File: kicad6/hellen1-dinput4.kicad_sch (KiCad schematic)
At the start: 9 parts

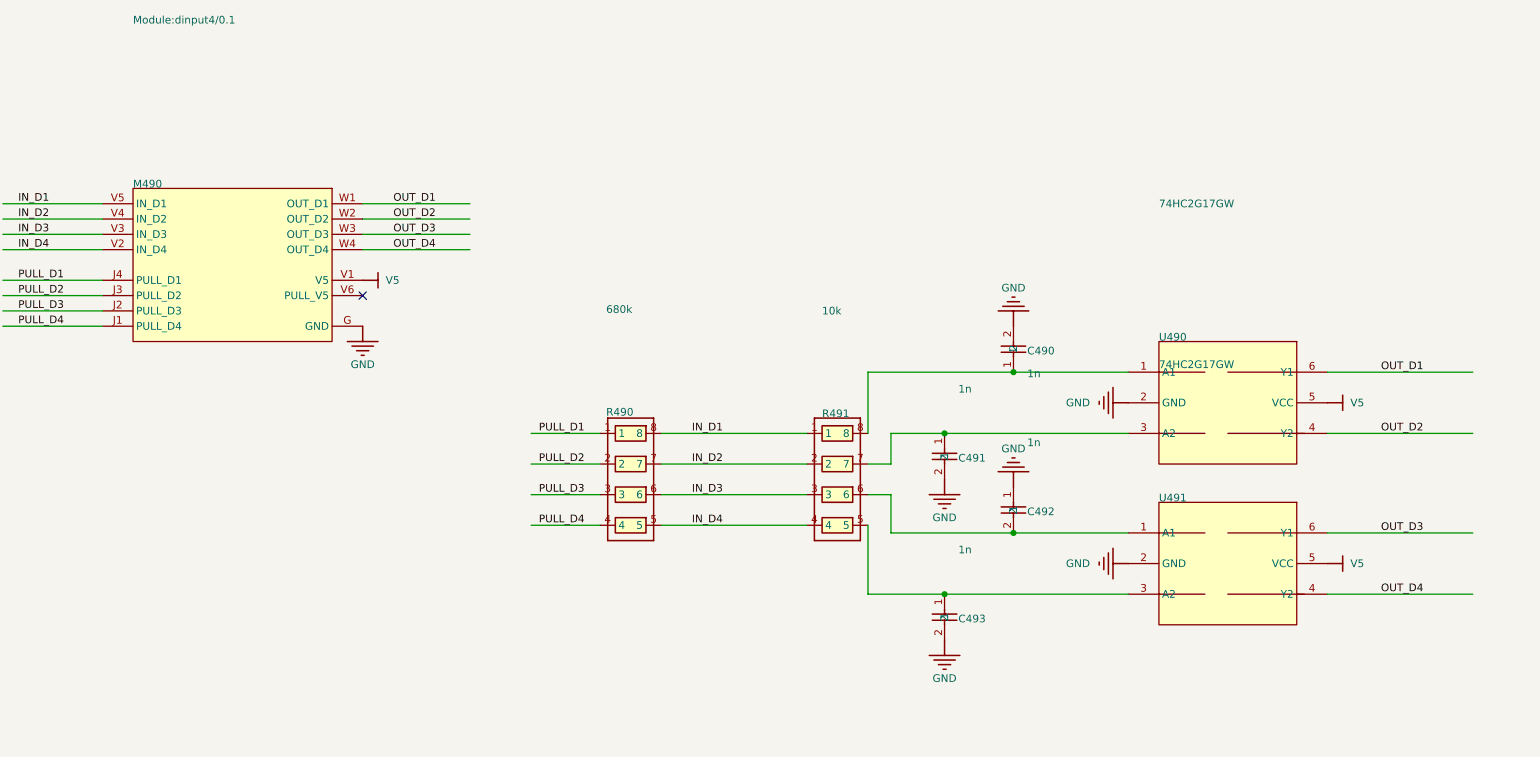
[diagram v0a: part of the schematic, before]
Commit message: move kicad src files into a separate folder
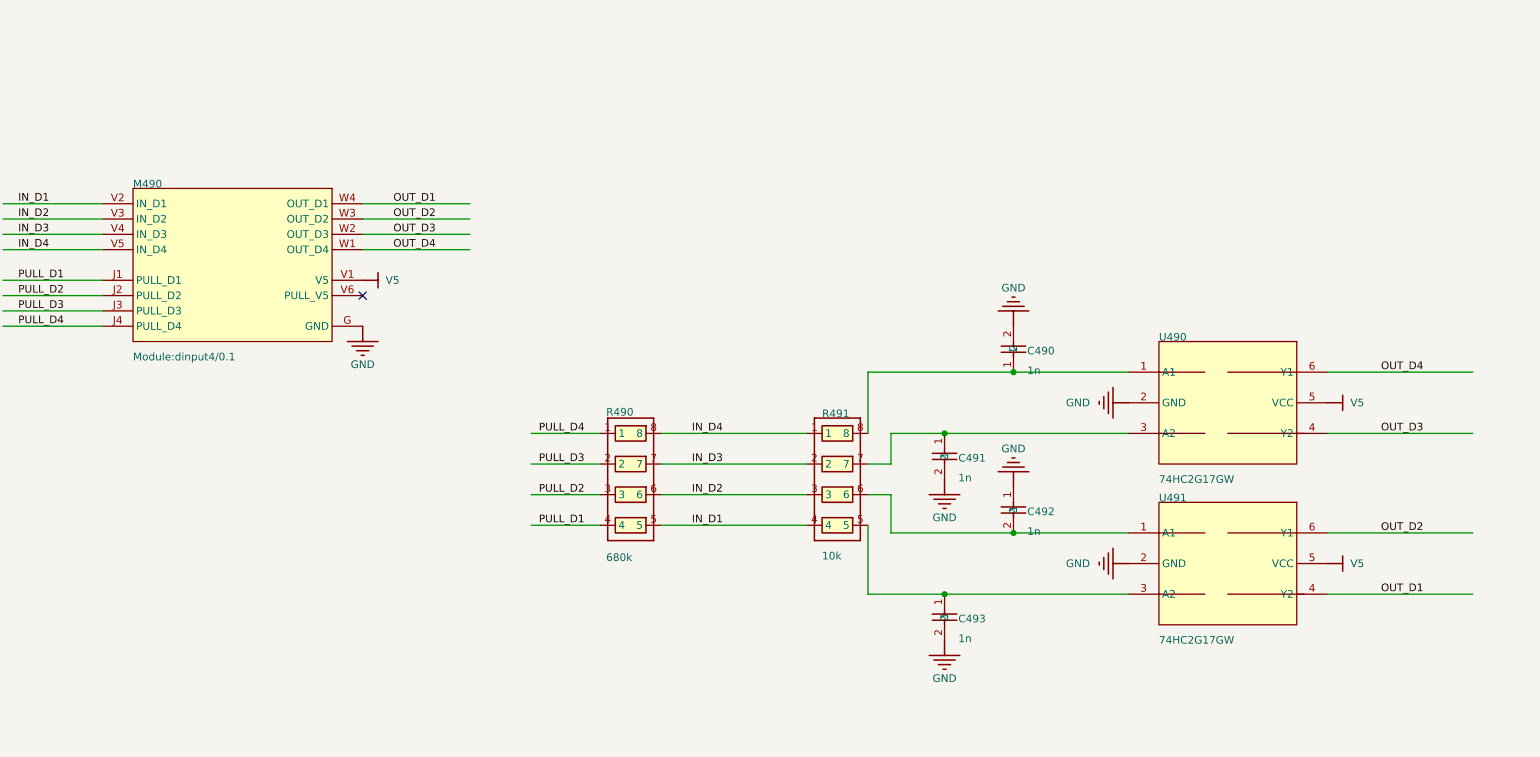
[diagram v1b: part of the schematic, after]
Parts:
- C490, C491, C492, C493: value (none) -> 1n; Comment 1n -> (none)
- M490: value (none) -> Module:dinput4/0.1; Comment Module:dinput4/0.1 -> (none)
- R490: value (none) -> 680k; Comment 680k -> (none)
- R491: value (none) -> 10k; Comment 10k -> (none)
- U490, U491: value (none) -> 74HC2G17GW; Comment 74HC2G17GW -> (none)
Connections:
- net IN_D1: now also M490.V2 (IN_D1), R490.5, R491.4; no longer M490.V5 (IN_D1), R490.8, R491.1
- net IN_D2: now also M490.V3 (IN_D2), R490.6, R491.3; no longer M490.V4 (IN_D2), R490.7, R491.2
- net IN_D3: now also M490.V4 (IN_D3), R490.7, R491.2; no longer M490.V3 (IN_D3), R490.6, R491.3
- net IN_D4: now also M490.V5 (IN_D4), R490.8, R491.1; no longer M490.V2 (IN_D4), R490.5, R491.4
- net OUT_D1: now also M490.W4 (OUT_D1), U491.4 (Y2); no longer M490.W1 (OUT_D1), U490.6 (Y1)
- net OUT_D2: now also M490.W3 (OUT_D2), U491.6 (Y1); no longer M490.W2 (OUT_D2), U490.4 (Y2)
- net OUT_D3: now also M490.W2 (OUT_D3), U490.4 (Y2); no longer M490.W3 (OUT_D3), U491.6 (Y1)
- net OUT_D4: now also M490.W1 (OUT_D4), U490.6 (Y1); no longer M490.W4 (OUT_D4), U491.4 (Y2)
- net PULL_D1: now also M490.J1 (PULL_D1), R490.4; no longer M490.J4 (PULL_D1), R490.1
- net PULL_D2: now also M490.J2 (PULL_D2), R490.3; no longer M490.J3 (PULL_D2), R490.2
- net PULL_D3: now also M490.J3 (PULL_D3), R490.2; no longer M490.J2 (PULL_D3), R490.3
- net PULL_D4: now also M490.J4 (PULL_D4), R490.1; no longer M490.J1 (PULL_D4), R490.4
